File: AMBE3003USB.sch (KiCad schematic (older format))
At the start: 96 parts, among them J1 McBSP, J2 ACONF, J3 CODEC, J4 USB_OTG, P1 CONFIG, U1 AMBE3003, U2 LD1117S33TR, U3 TPS3805, U4 FT232RL, U5 TPS78319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

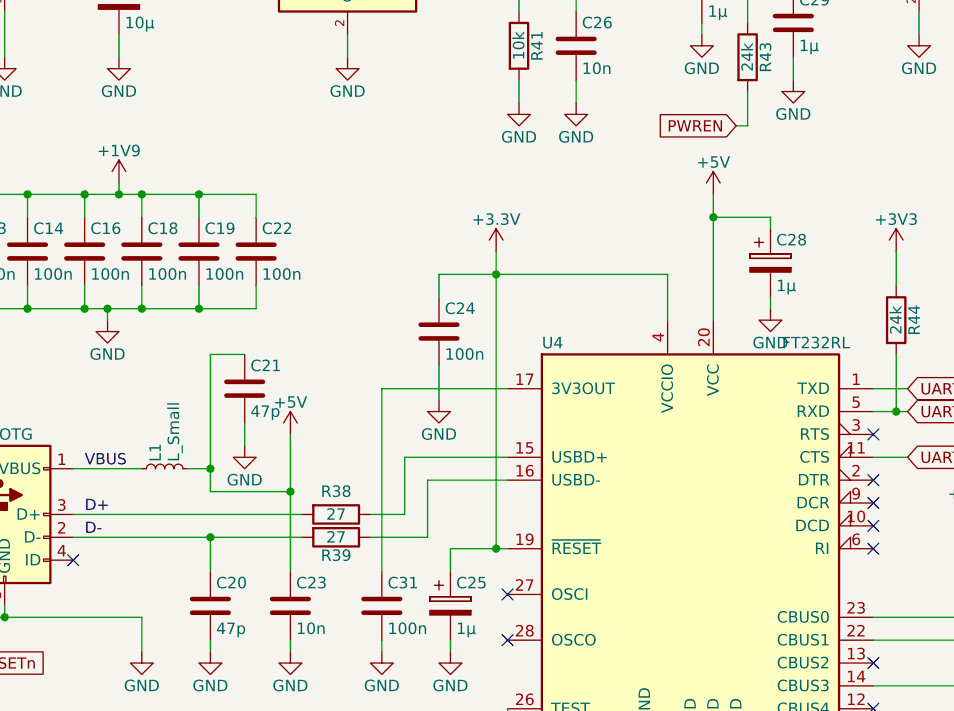
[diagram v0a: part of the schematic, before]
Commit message: Refactor schematic (moved C24)
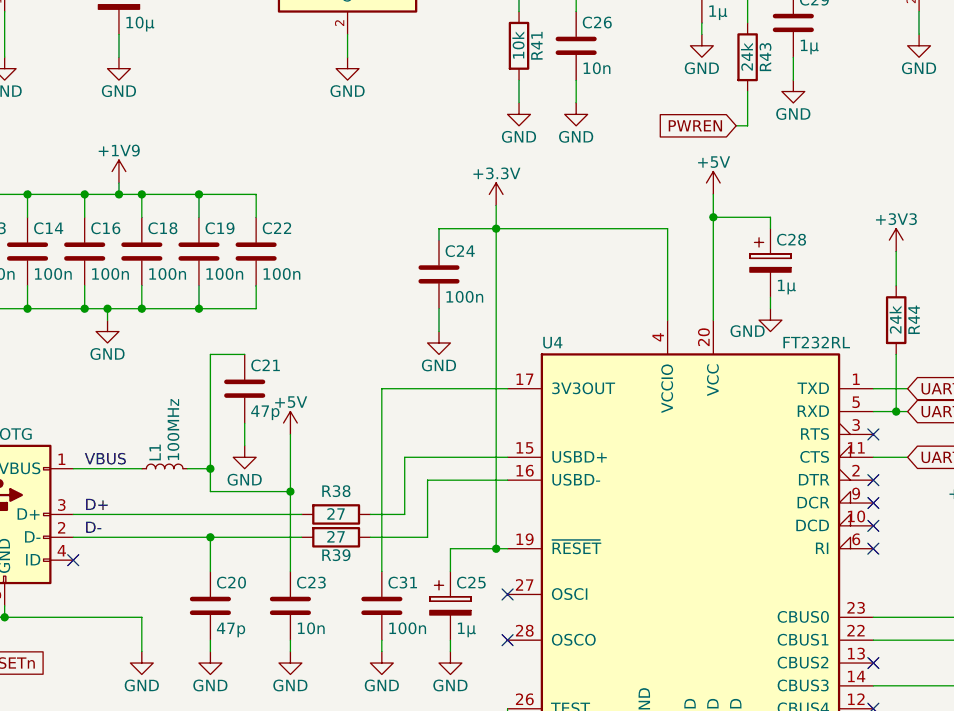
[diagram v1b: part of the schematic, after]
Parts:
- L1: value L_Small -> 100MHz
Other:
- moved on the sheet: C24
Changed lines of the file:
@@
 L C C24
 U 1 1 591C0987
-P 8200 2800
-F 0 "C24" H 8225 2900 50  0000 L CNN
-F 1 "100n" H 8225 2700 50  0000 L CNN
-F 2 "Capacitors_SMD:C_0603_HandSoldering" H 8238 2650 50  0001 C CNN
-F 3 "" H 8200 2800 50  0000 C CNN
-	1    8200 2800
+P 8200 2550
+F 0 "C24" H 8225 2650 50  0000 L CNN
+F 1 "100n" H 8225 2450 50  0000 L CNN
+F 2 "Capacitors_SMD:C_0603_HandSoldering" H 8238 2400 50  0001 C CNN
+F 3 "" H 8200 2550 50  0000 C CNN
+	1    8200 2550
 	1    0    0    -1
 $EndComp
@@
 L GND #PWR09
 U 1 1 591C1A11
-P 8200 3100
-F 0 "#PWR09" H 8200 2850 50  0001 C CNN
-F 1 "GND" H 8200 2950 50  0000 C CNN
-F 2 "" H 8200 3100 50  0000 C CNN
-F 3 "" H 8200 3100 50  0000 C CNN
-	1    8200 3100
+P 8200 2800
+F 0 "#PWR09" H 8200 2550 50  0001 C CNN
+F 1 "GND" H 8200 2650 50  0000 C CNN
+F 2 "" H 8200 2800 50  0000 C CNN
+F 3 "" H 8200 2800 50  0000 C CNN
+	1    8200 2800
 	1    0    0    -1
 $EndComp
@@
 L +3.3V #PWR026
 U 1 1 591DE698
-P 8450 2450
-F 0 "#PWR026" H 8450 2300 50  0001 C CNN
-F 1 "+3.3V" H 8450 2590 50  0000 C CNN
-F 2 "" H 8450 2450 50  0000 C CNN
-F 3 "" H 8450 2450 50  0000 C CNN
-	1    8450 2450
+P 8450 2250
+F 0 "#PWR026" H 8450 2100 50  0001 C CNN
+F 1 "+3.3V" H 8450 2390 50  0000 C CNN
+F 2 "" H 8450 2250 50  0000 C CNN
+F 3 "" H 8450 2250 50  0000 C CNN
+	1    8450 2250
 	1    0    0    -1
 $EndComp
@@
 P 9650 2700
 F 0 "#PWR028" H 9650 2450 50  0001 C CNN
-F 1 "GND" H 9650 2550 50  0000 C CNN
+F 1 "GND" H 9550 2600 50  0000 C CNN
 F 2 "" H 9650 2700 50  0000 C CNN
 F 3 "" H 9650 2700 50  0000 C CNN
@@
 P 7000 3400
 F 0 "L1" H 7030 3440 50  0000 L CNN
-F 1 "L_Small" H 7030 3360 50  0000 L CNN
+F 1 "100MHz" H 7030 3360 50  0000 L CNN
 F 2 "Inductors_SMD:L_0603_HandSoldering" H 7000 3400 50  0001 C CNN
 F 3 "" H 7000 3400 50  0000 C CNN
@@
 	7200 4150 7200 4200
 Wire Wire Line
-	8200 2950 8200 3100
-Wire Wire Line
 	7950 4200 7950 4150
 Wire Wire Line
@@
 	6700 1100 6800 1100
 Wire Wire Line
-	8450 2450 8450 3750
+	8450 2250 8450 3750
 Connection ~ 10500 4350
 Wire Wire Line
@@
 	8500 4450 8500 4850
 Wire Wire Line
-	9200 2550 9200 2750
+	9200 2350 9200 2750
 Wire Wire Line
 	8500 3350 8050 3350
@@
 	10750 2750 10750 2600
 Connection ~ 11000 2600
-Wire Wire Line
-	8200 2550 8200 2650
 Wire Wire Line
 	9500 4850 9500 4750
@@
 Connection ~ 3250 7150
 Wire Wire Line
-	8200 2550 9200 2550
-Wire Wire Line
 	3100 750  3100 900
 Wire Wire Line
@@
 Wire Wire Line
 	7350 3300 7350 3200
-Connection ~ 8450 2550
 Wire Wire Line
 	8250 3750 8500 3750
@@
 Text Label 5700 6400 0    49   ~ 0
 EC_ENABLE
+Wire Wire Line
+	8200 2400 8200 2350
+Wire Wire Line
+	8200 2350 9200 2350
+Connection ~ 8450 2350
+Wire Wire Line
+	8200 2800 8200 2700
 $EndSCHEMATC

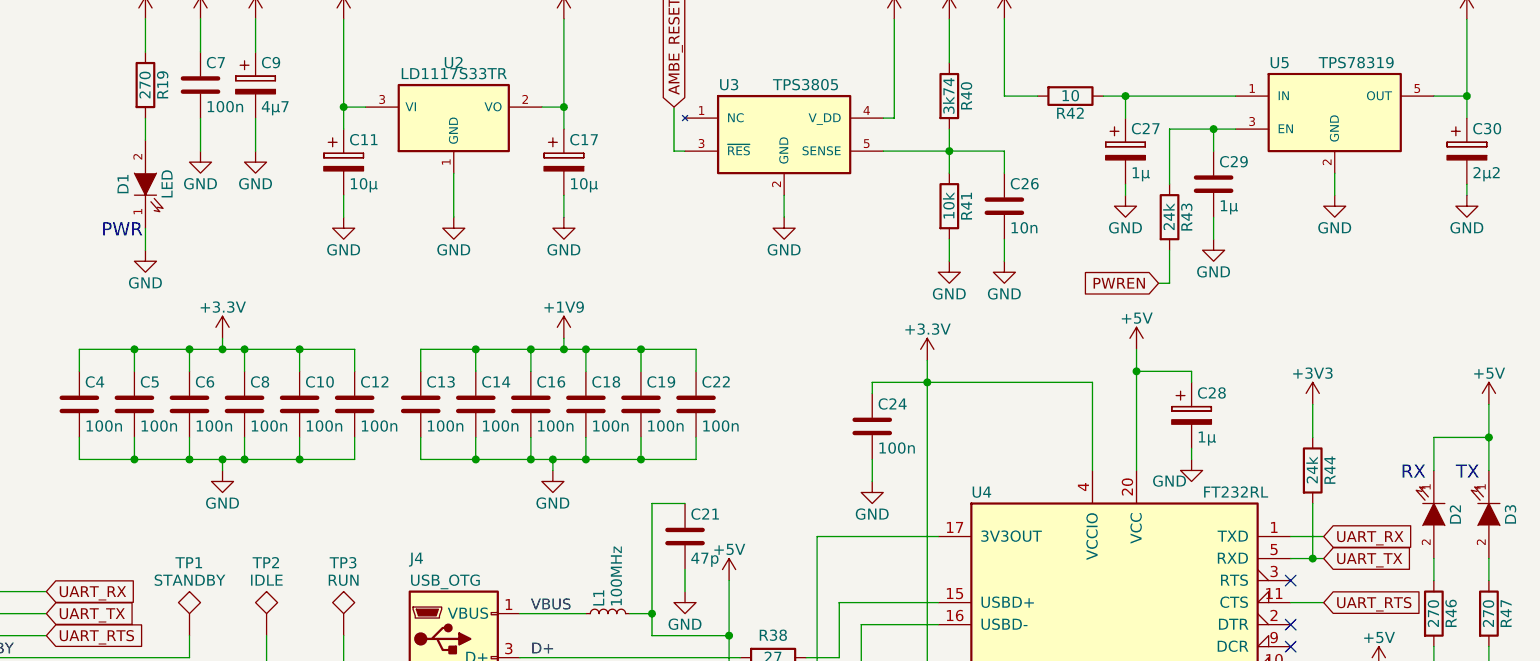
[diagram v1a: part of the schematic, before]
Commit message: Add LED colors and descriptors to board
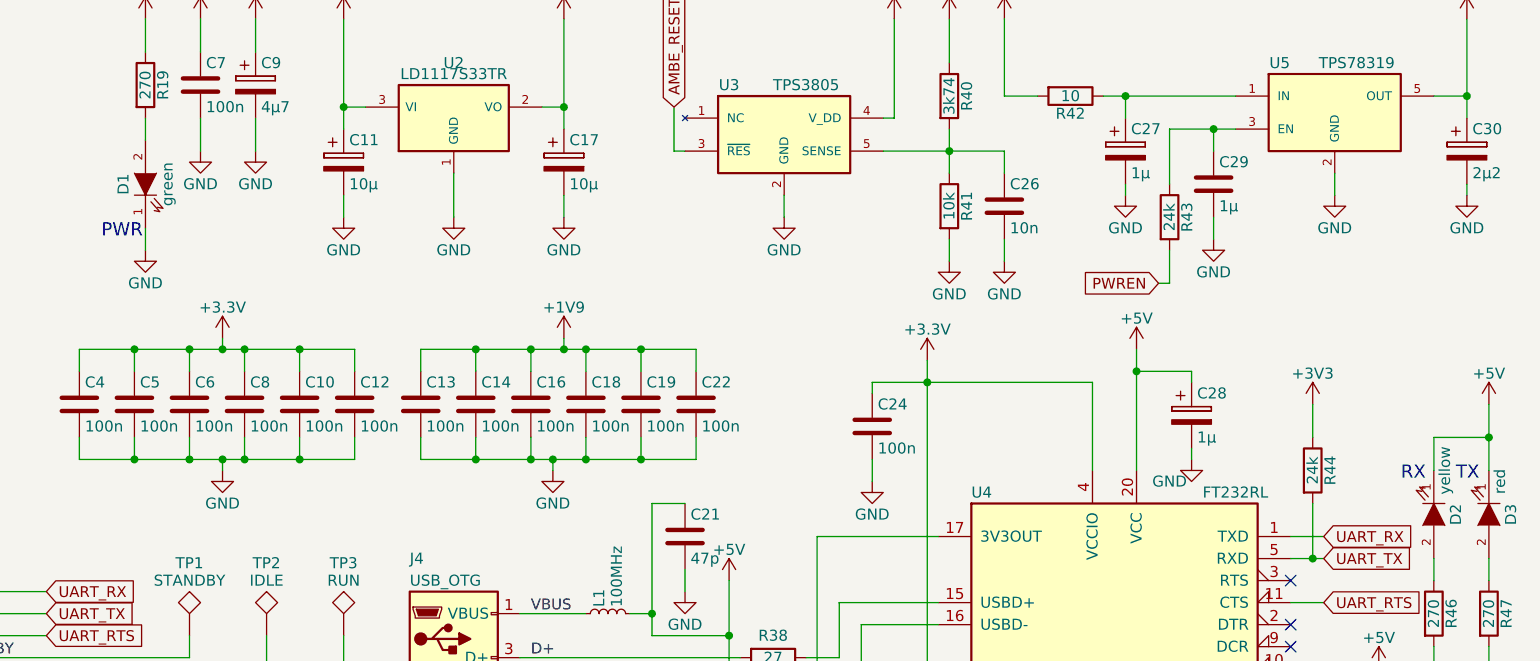
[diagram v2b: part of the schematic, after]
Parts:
- D1: value LED -> green
- D2: value LED -> yellow
- D3: value LED -> red
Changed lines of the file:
@@
 P 10750 2950
 F 0 "D2" H 10750 3050 50  0000 C CNN
-F 1 "LED" H 10750 2850 50  0001 C CNN
+F 1 "yellow" H 10550 3000 50  0000 C CNN
 F 2 "LEDs:LED_0603" H 10750 2950 50  0001 C CNN
 F 3 "" H 10750 2950 50  0000 C CNN
@@
 P 11000 2950
 F 0 "D3" H 11000 3050 50  0000 C CNN
-F 1 "LED" H 11000 2850 50  0001 C CNN
+F 1 "red" H 10850 3000 50  0000 C CNN
 F 2 "LEDs:LED_0603" H 11000 2950 50  0001 C CNN
 F 3 "" H 11000 2950 50  0000 C CNN
@@
 P 4900 1450
 F 0 "D1" H 4900 1550 50  0000 C CNN
-F 1 "LED" H 4900 1350 50  0000 C CNN
+F 1 "green" H 4900 1350 50  0000 C CNN
 F 2 "LEDs:LED_0603" H 4900 1450 50  0001 C CNN
 F 3 "" H 4900 1450 50  0000 C CNN

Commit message: Change footprint of USB connector
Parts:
- J4: footprint Connectors:USB_Mini-B -> Connect:USB_Mini-B
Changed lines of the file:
@@
 F 0 "J4" H 6100 4050 50  0000 L CNN
 F 1 "USB_OTG" H 6100 3950 50  0000 L CNN
-F 2 "Connectors:USB_Mini-B" H 6450 3550 50  0001 C CNN
+F 2 "Connect:USB_Mini-B" H 6450 3550 50  0001 C CNN
 F 3 "" H 6450 3550 50  0001 C CNN
 	1    6300 3600
@@
 F 0 "U1" H 1350 6600 60  0000 C CNN
 F 1 "AMBE3003" H 4200 6500 60  0000 C CNN
-F 2 "" H 2650 5800 60  0000 C CNN
+F 2 "" H 2650 5800 60  0001 C CNN
 F 3 "" H 2650 5800 60  0000 C CNN
 	1    2950 5250

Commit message: Add BOM for resistors
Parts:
- D1: MFR (none) -> Wurth Electronics; MPN (none) -> 150060VS75000; SPN (none) -> 710-150060VS75000; SPR (none) -> Mouser
- D2: MFR (none) -> Wurth Electronics; MPN (none) -> 150060YS75000; SPN (none) -> 710-150060YS75000; SPR (none) -> Mouser
- D3: MFR (none) -> Wurth Electronics; MPN (none) -> 150060SS75000; SPN (none) -> 710-150060SS75000; SPR (none) -> Mouser
- J4: MFR (none) -> Molex; MPN (none) -> 67503-1020; SPN (none) -> 538-67503-1020; SPR (none) -> Mouser
- L1: MFR (none) -> Murata Electronics; MPN (none) -> BLM18KG471BH1D; SPN (none) -> 81-BLM18KG471BH1D; SPR (none) -> Mouser
- R10, R11, R12, R13, R14, R15, R16, R17, R2, R3, R35, R36, R37, R4, R5, R6, R7, R8, R9: MFR (none) -> Yageo; MPN (none) -> RC0603FR-073K3L; SPN (none) -> 603-RC0603FR-073K3L; SPR (none) -> Mouser
- R18, R43, R44: MFR (none) -> Yageo; MPN (none) -> RC0603FR-0724KL; SPN (none) -> 603-RC0603FR-0724KL; SPR (none) -> Mouser
- R19, R46, R47: MFR (none) -> Yageo; MPN (none) -> RC0603FR-07270RL; SPN (none) -> 603-RC0603FR-07270RL; SPR (none) -> Mouser
- R20, R21, R22, R23, R24, R25, R26, R27, R28, R29, R30, R31, R32, R33: MFR (none) -> Yageo; MPN (none) -> RC0603FR-070RL; SPN (none) -> 603-RC0603FR-070RL; SPR (none) -> Mouser
- R38, R39: MFR (none) -> Yageo; MPN (none) -> RC0603FR-0727RL; SPN (none) -> 603-RC0603FR-0727RL; SPR (none) -> Mouser
- R40: MFR (none) -> Yageo; MPN (none) -> RC0603FR-073K74L; SPN (none) -> 603-RC0603FR-073K74L; SPR (none) -> Mouser
- R41, R45: MFR (none) -> Yageo; MPN (none) -> AR0603FR-0710KL; SPN (none) -> 603-AR0603FR-0710KL; SPR (none) -> Mouser
- R42: MFR (none) -> Yageo; MPN (none) -> RC0603FR-0710RL; SPN (none) -> 603-RC0603FR-0710RL; SPR (none) -> Mouser

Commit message: Add BOM for 5.1 resistor
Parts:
- R1, R34: MFR (none) -> Yageo; MPN (none) -> RC0603FR-075R11L; SPN (none) -> 603-RC0603FR-075R11L; SPR (none) -> Mouser
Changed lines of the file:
@@
 F 1 "5.1" V 700 4100 50 0000 C CNN
 F 2 "Resistors_SMD:R_0603_HandSoldering" V 630 4100 50 0001 C CNN
-F 3 "" H 700 4100 50 0001 C CNN
-F 4 "" H 0 0 50 0001 C CNN "MFR"
-F 5 "" H 0 0 50 0001 C CNN "MPN"
-F 6 "" H 0 0 50 0001 C CNN "SPR"
-F 7 "" H 0 0 50 0001 C CNN "SPN"
+F 3 "http://www.mouser.com/ds/2/447/RC0603-272842.pdf" H 700 4100 50 0001 C CNN
+F 4 "Yageo" H 0 0 50 0001 C CNN "MFR"
+F 5 "RC0603FR-075R11L" H 0 0 50 0001 C CNN "MPN"
+F 6 "Mouser" H 0 0 50 0001 C CNN "SPR"
+F 7 "603-RC0603FR-075R11L" H 0 0 50 0001 C CNN "SPN"
 F 8 "" H 0 0 50 0001 C CNN "SPURL"
 	1    700  4100
@@
 F 1 "5.1" V 5450 6800 50 0000 C CNN
 F 2 "Resistors_SMD:R_0603_HandSoldering" V 5380 6800 50 0001 C CNN
-F 3 "" H 5450 6800 50 0001 C CNN
-F 4 "" H 0 0 50 0001 C CNN "MFR"
-F 5 "" H 0 0 50 0001 C CNN "MPN"
-F 6 "" H 0 0 50 0001 C CNN "SPR"
-F 7 "" H 0 0 50 0001 C CNN "SPN"
+F 3 "http://www.mouser.com/ds/2/447/RC0603-272842.pdf" H 5450 6800 50 0001 C CNN
+F 4 "Yageo" H 0 0 50 0001 C CNN "MFR"
+F 5 "RC0603FR-075R11L" H 0 0 50 0001 C CNN "MPN"
+F 6 "Mouser" H 0 0 50 0001 C CNN "SPR"
+F 7 "603-RC0603FR-075R11L" H 0 0 50 0001 C CNN "SPN"
 F 8 "" H 0 0 50 0001 C CNN "SPURL"
 	1    5450 6800

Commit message: Add BOM for ICs
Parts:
- U2: MFR (none) -> STMicroelectronics; MPN (none) -> LD1117S33TR; SPN (none) -> 511-LD1117S33; SPR (none) -> Mouser
- U3: MFR (none) -> Texas Instruments; MPN (none) -> TPS3805H33DCKR; SPN (none) -> 595-TPS3805H33DCKR; SPR (none) -> Mouser
- U5: MFR (none) -> Texas Instruments; MPN (none) -> TPS78319DDCR; SPN (none) -> 595-TPS78319DDCR; SPR (none) -> Mouser
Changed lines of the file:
@@
 F 1 "LD1117S33TR" H 6300 1350 50 0000 C CNN
 F 2 "TO_SOT_Packages_SMD:SOT-223-3Lead_TabPin2" H 6300 1250 50 0001 C CNN
-F 3 "" H 6300 1150 50 0001 C CNN
-F 4 "" H 0 0 50 0001 C CNN "MFR"
-F 5 "" H 0 0 50 0001 C CNN "MPN"
-F 6 "" H 0 0 50 0001 C CNN "SPR"
-F 7 "" H 0 0 50 0001 C CNN "SPN"
+F 3 "http://www.mouser.com/ds/2/389/ld1117-974075.pdf" H 6300 1150 50 0001 C CNN
+F 4 "STMicroelectronics" H 0 0 50 0001 C CNN "MFR"
+F 5 "LD1117S33TR" H 0 0 50 0001 C CNN "MPN"
+F 6 "Mouser" H 0 0 50 0001 C CNN "SPR"
+F 7 "511-LD1117S33" H 0 0 50 0001 C CNN "SPN"
 F 8 "" H 0 0 50 0001 C CNN "SPURL"
 	1    6300 1150
@@
 F 1 "TPS78319" H 10400 1300 50 0000 C CNN
 F 2 "TO_SOT_Packages_SMD:SOT-23-5_HandSoldering" H 10300 1200 50 0001 C CIN
-F 3 "" H 10300 1100 50 0000 C CNN
-F 4 "" H 0 0 50 0001 C CNN "MFR"
-F 5 "" H 0 0 50 0001 C CNN "MPN"
-F 6 "" H 0 0 50 0001 C CNN "SPR"
-F 7 "" H 0 0 50 0001 C CNN "SPN"
+F 3 "http://www.ti.com/lit/gpn/tps783" H 10300 1100 50 0001 C CNN
+F 4 "Texas Instruments" H 0 0 50 0001 C CNN "MFR"
+F 5 "TPS78319DDCR" H 0 0 50 0001 C CNN "MPN"
+F 6 "Mouser" H 0 0 50 0001 C CNN "SPR"
+F 7 "595-TPS78319DDCR" H 0 0 50 0001 C CNN "SPN"
 F 8 "" H 0 0 50 0001 C CNN "SPURL"
 	1    10300 1100
@@
 F 1 "TPS3805" H 7900 1400 50 0000 C CNN
 F 2 "TI:DCK" H 7800 1300 50 0001 C CIN
-F 3 "" H 7800 1200 50 0000 C CNN
-F 4 "" H 0 0 50 0001 C CNN "MFR"
-F 5 "" H 0 0 50 0001 C CNN "MPN"
-F 6 "" H 0 0 50 0001 C CNN "SPR"
-F 7 "" H 0 0 50 0001 C CNN "SPN"
+F 3 "http://www.ti.com/lit/gpn/tps3805h33" H 7800 1200 50 0001 C CNN
+F 4 "Texas Instruments" H 0 0 50 0001 C CNN "MFR"
+F 5 "TPS3805H33DCKR" H 0 0 50 0001 C CNN "MPN"
+F 6 "Mouser" H 0 0 50 0001 C CNN "SPR"
+F 7 "595-TPS3805H33DCKR" H 0 0 50 0001 C CNN "SPN"
 F 8 "" H 0 0 50 0001 C CNN "SPURL"
 	1    7800 1200

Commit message: Add BOM for pin headers
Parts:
- J1: MFR (none) -> Harwin; MPN (none) -> M20-9980446; SPN (none) -> 855-M20-9980446; SPR (none) -> Mouser
- J2: MFR (none) -> Harwin; MPN (none) -> M20-9980346; SPN (none) -> 855-M20-9980346; SPR (none) -> Mouser
- J3: MFR (none) -> Harwin; MPN (none) -> M20-9980546; SPN (none) -> 855-M20-9980546; SPR (none) -> Mouser
- P1: MFR (none) -> Harwin; MPN (none) -> M20-9981646; SPN (none) -> 855-M20-9981646; SPR (none) -> Mouser
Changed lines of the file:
@@
 F 1 "CONFIG" V 2350 1150 50 0000 C CNN
 F 2 "Pin_Headers:Pin_Header_Straight_2x16_Pitch2.54mm" H 2350 50 50 0001 C CNN
-F 3 "" H 2350 50 50 0000 C CNN
-F 4 "" H 0 0 50 0001 C CNN "MFR"
-F 5 "" H 0 0 50 0001 C CNN "MPN"
-F 6 "" H 0 0 50 0001 C CNN "SPR"
-F 7 "" H 0 0 50 0001 C CNN "SPN"
+F 3 "http://www.mouser.com/ds/2/181/M20-998-351176.pdf" H 2350 50 50 0001 C CNN
+F 4 "Harwin" H 0 0 50 0001 C CNN "MFR"
+F 5 "M20-9981646" H 0 0 50 0001 C CNN "MPN"
+F 6 "Mouser" H 0 0 50 0001 C CNN "SPR"
+F 7 "855-M20-9981646" H 0 0 50 0001 C CNN "SPN"
 F 8 "" H 0 0 50 0001 C CNN "SPURL"
 	1    2350 1150
@@
 F 1 "McBSP" V 5500 4400 50 0000 C CNN
 F 2 "Pin_Headers:Pin_Header_Straight_2x04_Pitch2.54mm" H 5500 3200 50 0001 C CNN
-F 3 "" H 5500 3200 50 0001 C CNN
-F 4 "" H 0 0 50 0001 C CNN "MFR"
-F 5 "" H 0 0 50 0001 C CNN "MPN"
-F 6 "" H 0 0 50 0001 C CNN "SPR"
-F 7 "" H 0 0 50 0001 C CNN "SPN"
+F 3 "http://www.mouser.com/ds/2/181/M20-998-351176.pdf" H 5500 3200 50 0001 C CNN
+F 4 "Harwin" H 0 0 50 0001 C CNN "MFR"
+F 5 "M20-9980446" H 0 0 50 0001 C CNN "MPN"
+F 6 "Mouser" H 0 0 50 0001 C CNN "SPR"
+F 7 "855-M20-9980446" H 0 0 50 0001 C CNN "SPN"
 F 8 "" H 0 0 50 0001 C CNN "SPURL"
 	1    5500 4400
@@
 F 1 "ACONF" V 6450 6300 50 0000 C CNN
 F 2 "Pin_Headers:Pin_Header_Straight_2x03_Pitch2.54mm" H 6450 5100 50 0001 C CNN
-F 3 "" H 6450 5100 50 0001 C CNN
-F 4 "" H 0 0 50 0001 C CNN "MFR"
-F 5 "" H 0 0 50 0001 C CNN "MPN"
-F 6 "" H 0 0 50 0001 C CNN "SPR"
-F 7 "" H 0 0 50 0001 C CNN "SPN"
+F 3 "http://www.mouser.com/ds/2/181/M20-998-351176.pdf" H 6450 5100 50 0001 C CNN
+F 4 "Harwin" H 0 0 50 0001 C CNN "MFR"
+F 5 "M20-9980346" H 0 0 50 0001 C CNN "MPN"
+F 6 "Mouser" H 0 0 50 0001 C CNN "SPR"
+F 7 "855-M20-9980346" H 0 0 50 0001 C CNN "SPN"
 F 8 "" H 0 0 50 0001 C CNN "SPURL"
 	1    6450 6300
@@
 F 1 "CODEC" V 7600 5600 50 0000 C CNN
 F 2 "Pin_Headers:Pin_Header_Straight_2x05_Pitch2.54mm" H 7600 4400 50 0001 C CNN
-F 3 "" H 7600 4400 50 0001 C CNN
-F 4 "" H 0 0 50 0001 C CNN "MFR"
-F 5 "" H 0 0 50 0001 C CNN "MPN"
-F 6 "" H 0 0 50 0001 C CNN "SPR"
-F 7 "" H 0 0 50 0001 C CNN "SPN"
+F 3 "http://www.mouser.com/ds/2/181/M20-998-351176.pdf" H 7600 4400 50 0001 C CNN
+F 4 "Harwin" H 0 0 50 0001 C CNN "MFR"
+F 5 "M20-9980546" H 0 0 50 0001 C CNN "MPN"
+F 6 "Mouser" H 0 0 50 0001 C CNN "SPR"
+F 7 "855-M20-9980546" H 0 0 50 0001 C CNN "SPN"
 F 8 "" H 0 0 50 0001 C CNN "SPURL"
 	1    7600 5600

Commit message: Add BOM for FT232RL
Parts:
- U4: MFR (none) -> FTDI; MPN (none) -> FT232RL-REEL; SPN (none) -> 895-FT232RL; SPR (none) -> Mouser
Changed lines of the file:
@@
 F 1 "FT232RL" H 9700 4650 50 0000 L CNN
 F 2 "Housings_SSOP:SSOP-28_5.3x10.2mm_Pitch0.65mm" H 9350 2250 50 0001 C CNN
-F 3 "" H 9300 3750 50 0001 C CNN
-F 4 "" H 0 0 50 0001 C CNN "MFR"
-F 5 "" H 0 0 50 0001 C CNN "MPN"
-F 6 "" H 0 0 50 0001 C CNN "SPR"
-F 7 "" H 0 0 50 0001 C CNN "SPN"
+F 3 "http://www.mouser.com/ds/2/163/DS_FT232R-11534.pdf" H 9300 3750 50 0001 C CNN
+F 4 "FTDI" H 0 0 50 0001 C CNN "MFR"
+F 5 "FT232RL-REEL" H 0 0 50 0001 C CNN "MPN"
+F 6 "Mouser" H 0 0 50 0001 C CNN "SPR"
+F 7 "895-FT232RL" H 0 0 50 0001 C CNN "SPN"
 F 8 "" H 0 0 50 0001 C CNN "SPURL"
 	1    9300 3750
